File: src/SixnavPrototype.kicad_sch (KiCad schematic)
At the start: 33 parts, among them Q1 PT908-7C-F, Q2 PT908-7C-F, Q3 PT908-7C-F, Q4 PT908-7C-F, Q5 PT908-7C-F, Q6 PT908-7C-F, U1 Pico, U2 CD4051B

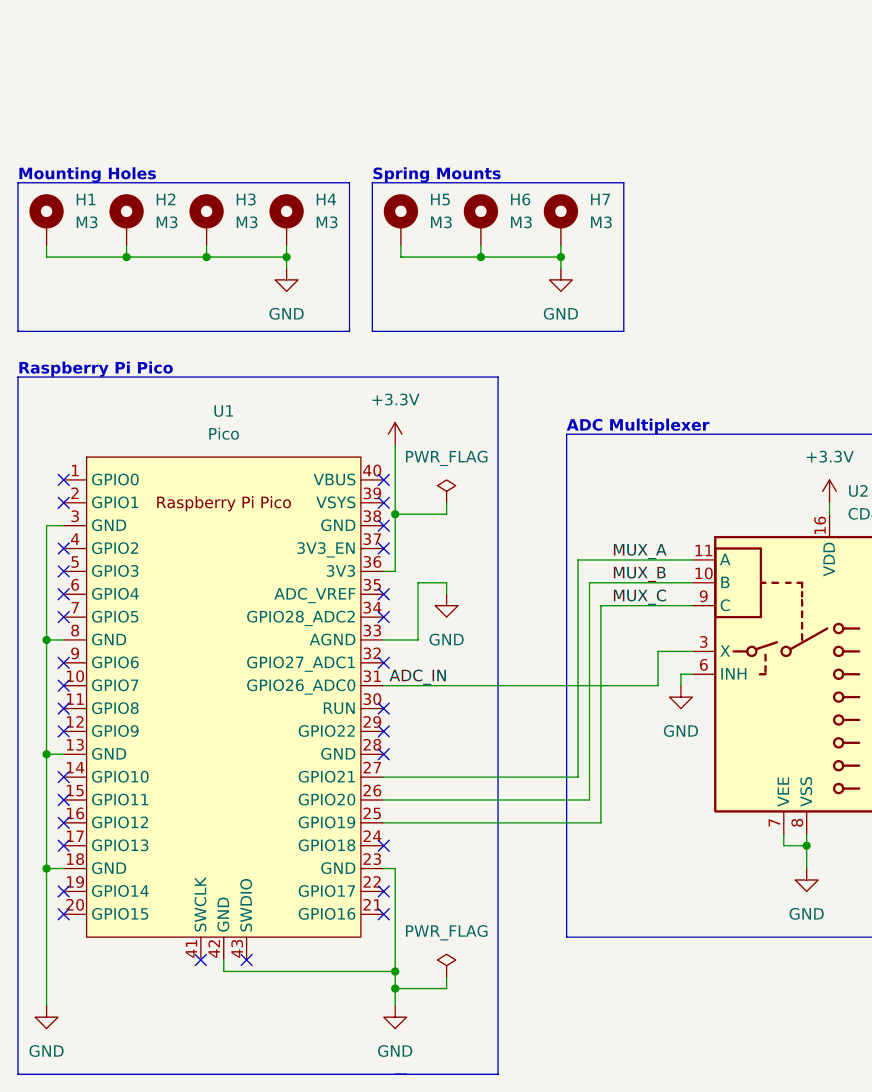
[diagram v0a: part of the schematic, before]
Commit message: Replaced symbols, footprints, models, with lib
Internal libraries also fix the reversed phototransistor issue.
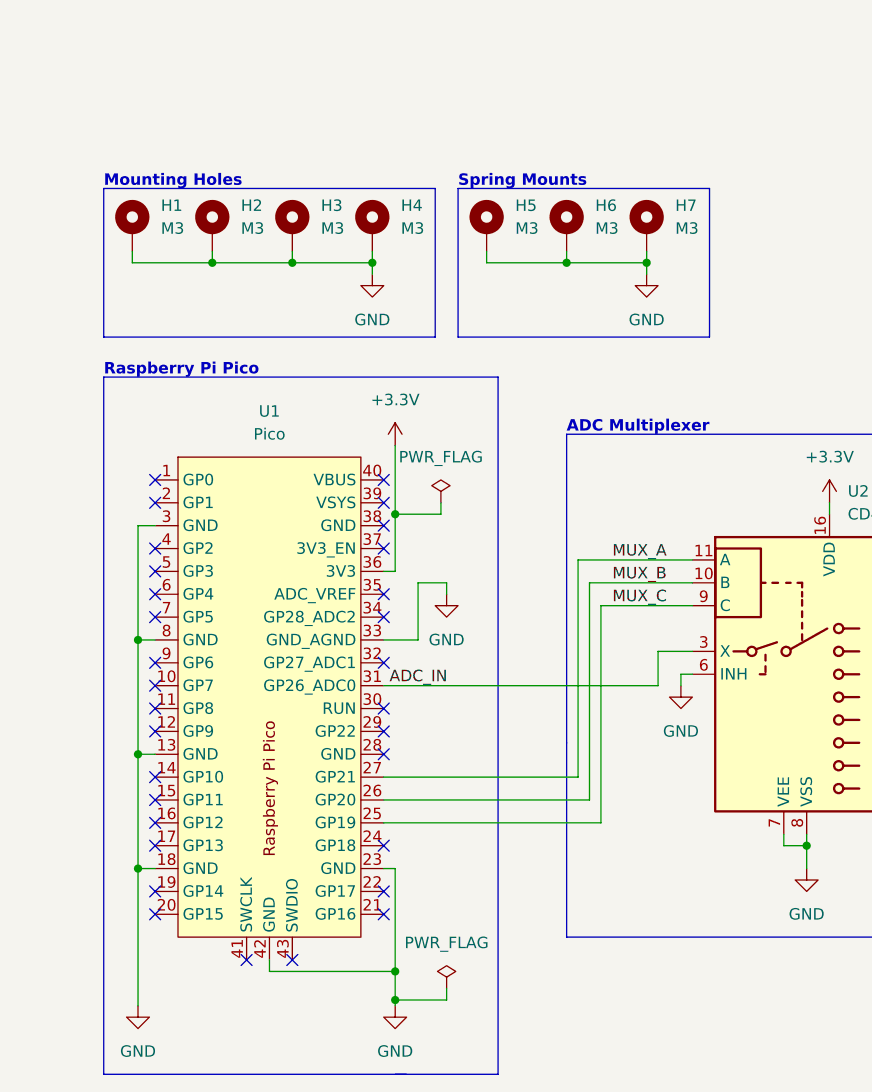
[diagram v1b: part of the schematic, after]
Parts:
- U1: symbol MCU_RaspberryPi_and_Boards:Pico -> LibSixnavPrototype:Raspberry_Pi_Pico
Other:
- moved on the sheet: H1, H2, H3, H4, H5, H6, H7, U1

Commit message: add symbols, fix LED polarity
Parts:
- D1, D2, D3, D4, D5, D6: footprint SamacSys_Parts:IR9087CF -> LibSixnavPrototype:IR908-7C-F; symbol Device:LED -> LibSixnavPrototype:IR908-7C-F
- Q1, Q2, Q3, Q4, Q5, Q6: footprint SamacSys_Parts:ELPT9087C -> LibSixnavPrototype:PT908-7C-F; symbol Device:Q_Photo_NPN_EC -> LibSixnavPrototype:PT908-7C-F
- U1: footprint MCU_RaspberryPi_and_Boards:RPi_Pico_SMD_TH -> LibSixnavPrototype:Raspberry Pi Pico
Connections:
- net D1_A: now also D1.1 (A); no longer D1.2 (A)
- net D2_A: now also D2.1 (A); no longer D2.2 (A)
- net D3_A: now also D3.1 (A); no longer D3.2 (A)
- net D4_A: now also D4.1 (A); no longer D4.2 (A)
- net D5_A: now also D5.1 (A); no longer D5.2 (A)
- net D6_A: now also D6.1 (A); no longer D6.2 (A)
- net GND: now also D1.2 (K), D2.2 (K), D3.2 (K), D4.2 (K), D5.2 (K), D6.2 (K); no longer D1.1 (K), D2.1 (K), D3.1 (K), D4.1 (K), D5.1 (K), D6.1 (K)
